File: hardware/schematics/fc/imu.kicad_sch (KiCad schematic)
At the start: 3 parts, among them U6 LSM6DSV16XTR

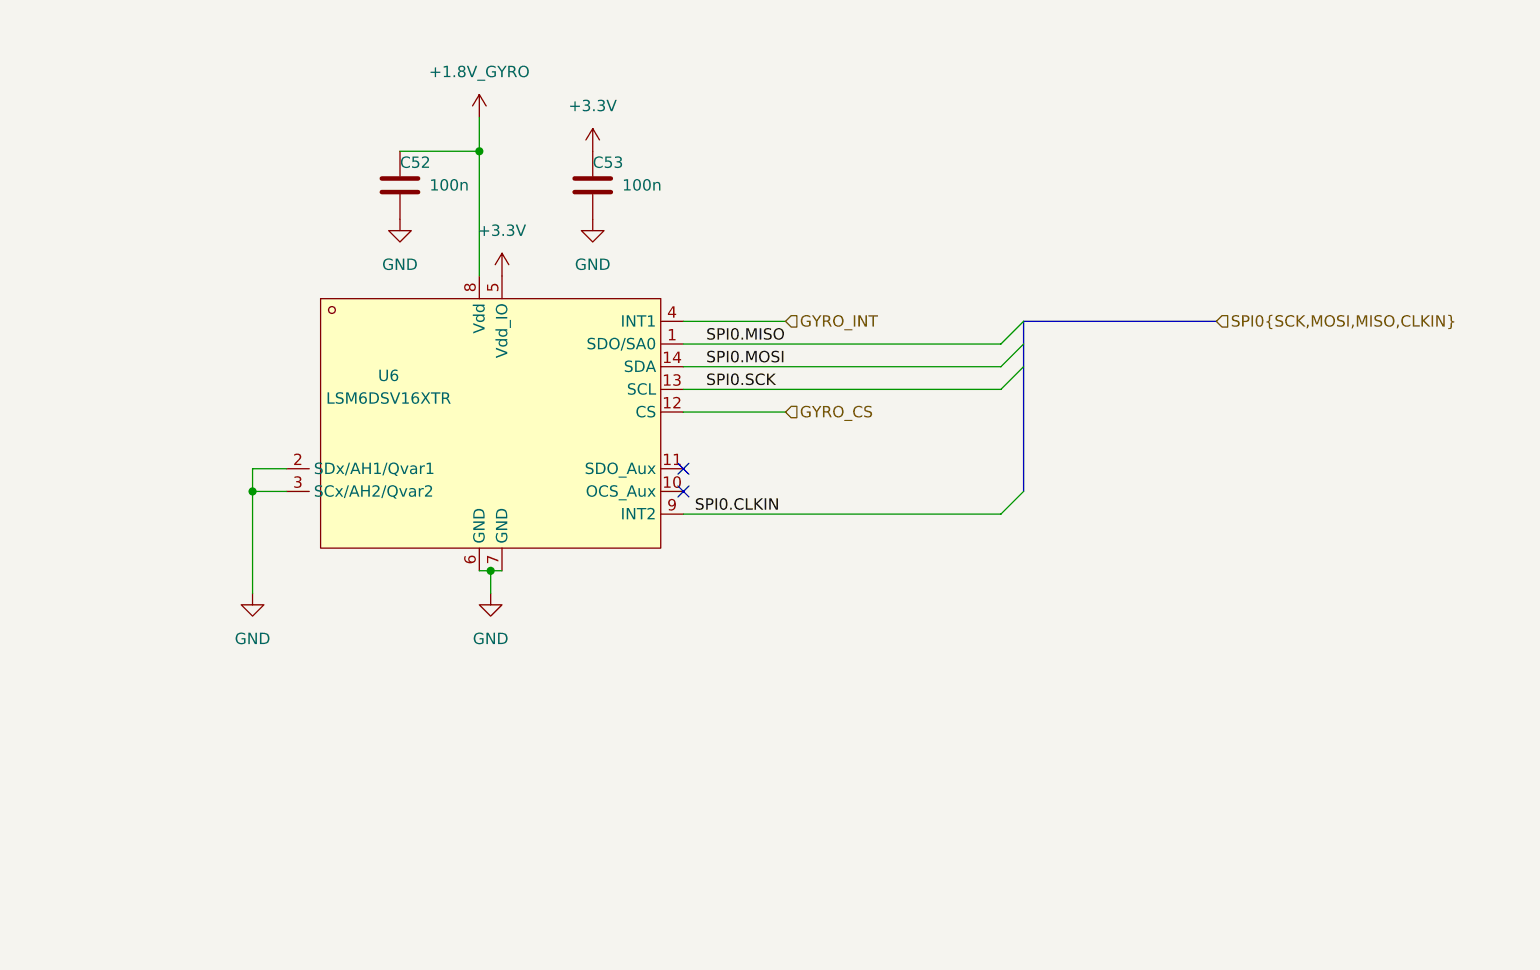
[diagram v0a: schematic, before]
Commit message: Refresh design sources: import rev2 sheets + libs from current sibling repos
FC sheets   <- OpenFC-Lite-Mini rev2 (RP2354A, LMR51430 power tree, COS8051 OSD)
ESC sheets  <- 4in1-mini Rev2 (AT32F421 + NSG2065Q + DOY180N03T, INA186 CSA)
ELRS sheet  <- OpenRX-Lite (ESP32-C3 + SX1281, chip antenna)

Drop-in swaps at paths the root sheet already references; esc_channel
instantiated 4x from root resolves. esc_main.kicad_sch (4in1-mini top:
buck/LDO/CSA/TVS/connector) kept as reference, with ESC.kicad_sch beside
it so its internal channel instances resolve if ever instantiated.

Libraries replaced wholesale: lib(.kicad_sym/.pretty/.3dshapes) from
OpenFC-Lite-Mini, components+4in1ESC from 4in1-mini, OpenRX-Shared from
OpenRX. 3D model paths in OpenRX-Shared.pretty rewritten to project-
local via pcbnew API. Hierarchy verified with kicad-cli netlist export.

Supersedes the 2026-04 port from OpenFC-ECO V0.3 / 4in1ESC 2 (in git
history). Schematic re-annotation + root rewiring is manual work in
KiCad. Old PCB layout retained; footprints are embedded so it opens,
but layout predates this refresh.

Co-Authored-By: Claude Fable 5 <noreply@anthropic.com>
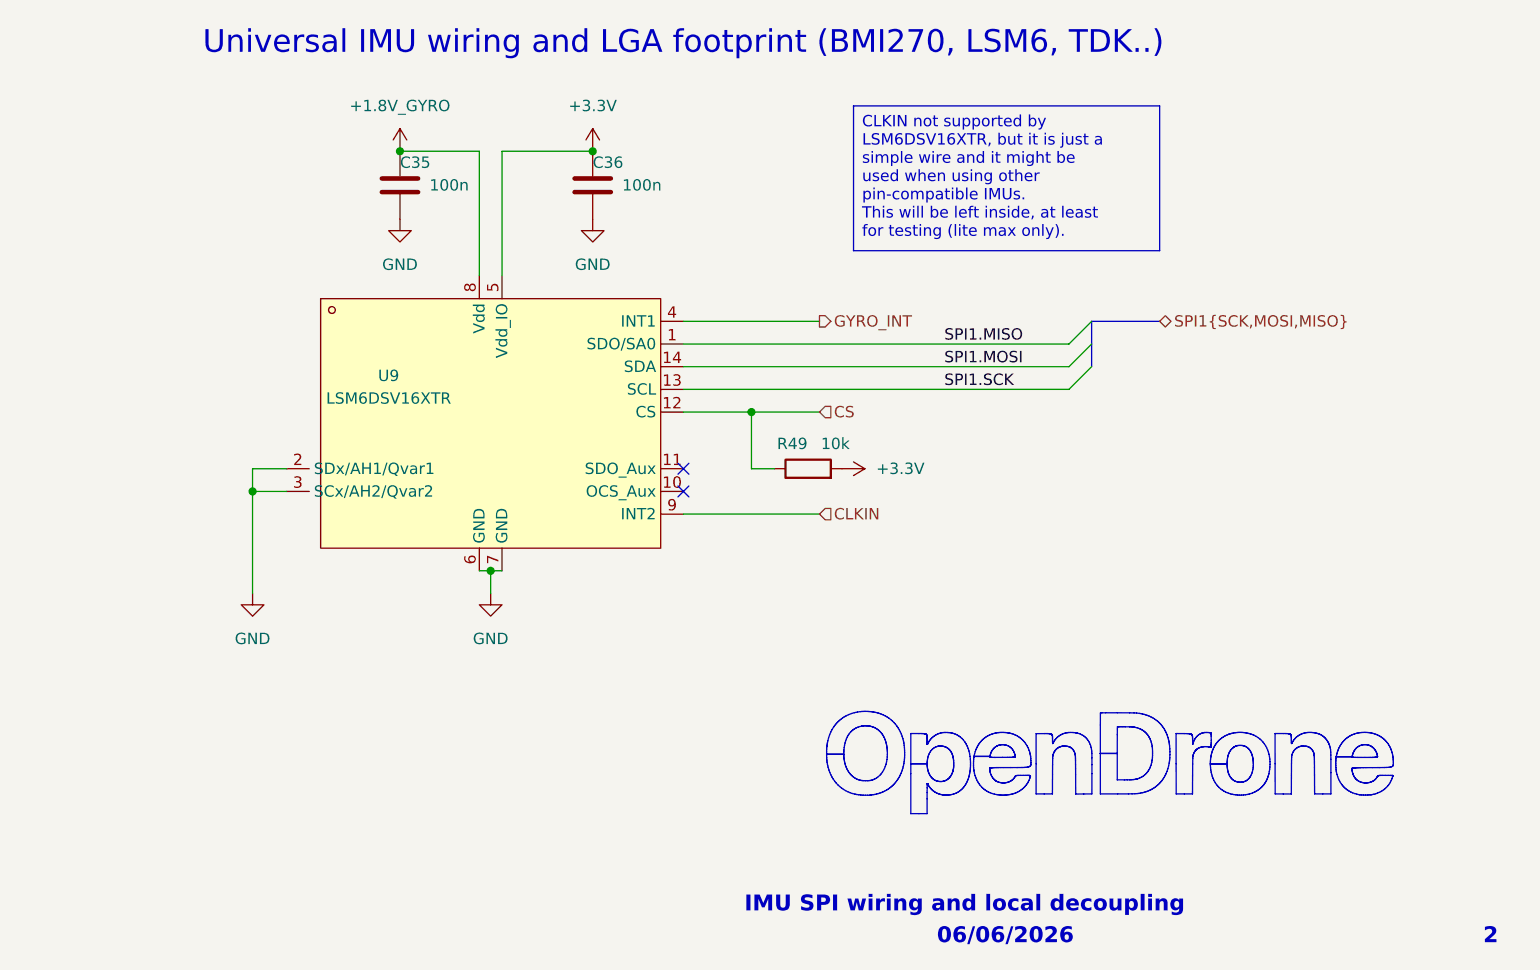
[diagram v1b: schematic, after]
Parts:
- added R49: 10k, Resistor_SMD:R_0201_0603Metric, symbol Device:R
- U9: renamed from U6; LCSC (none) -> C5267406; LCSC Part C5267406 -> (none)
- renumbered C52 to C35, C53 to C36
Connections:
- net +3.3V: now also R49.2
- net GYRO_CS renamed CS
- net CS: now also R49.1
- net SPI0.CLKIN renamed CLKIN
- net SPI0.MISO renamed SPI1.MISO
- net SPI0.MOSI renamed SPI1.MOSI
- net SPI0.SCK renamed SPI1.SCK
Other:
- note added: "06/06/2026"
- note added: "2"
- note added: "IMU SPI wiring and local decoupling"
- note added: "Universal IMU wiring and LGA footprint (BMI270, LSM6, TDK..)"
